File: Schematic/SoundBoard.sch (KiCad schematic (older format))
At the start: 0 parts

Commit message: Inital rev 1.0 commit
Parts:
- added C? (x8): 100n, symbol Device:C
- added C?: 10u, symbol Device:C
- added C? (x3): C, symbol Device:C
- added C? (x2): 2.2u, symbol Device:C
- added D?: D_Schottky, symbol Device:D_Schottky
- added D? (x3): LED, symbol Device:LED
- added F?: Fuse, symbol Device:Fuse
- added FB?: Ferrite_Bead, symbol Device:Ferrite_Bead
- added H? (x4): MountingHole_Pad, symbol Mechanical:MountingHole_Pad
- added J?: Conn_ARM_JTAG_SWD_10, symbol Connector:Conn_ARM_JTAG_SWD_10
- added LS?: Speaker, symbol Device:Speaker
- added R? (x5): R, symbol Device:R
- added SW? (x2): SW_Push, symbol Switch:SW_Push
- added U?: STM32F405RGTx, Package_QFP:LQFP-64_10x10mm_P0.5mm, symbol MCU_ST_STM32F4:STM32F405RGTx
- added U?: AMS1117-3.3, Package_TO_SOT_SMD:SOT-223-3_TabPin2, symbol Regulator_Linear:AMS1117-3.3
- added U? (x3): LM4562, symbol Amplifier_Operational:LM4562
- added U?: CS4344-CZZR, symbol SoundBoard:CS4344-CZZR
- added U?: W25Q128JVS, Package_SO:SOIC-8_5.23x5.23mm_P1.27mm, symbol Memory_Flash:W25Q128JVS
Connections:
- new net: C?.1, U?.31 (VCAP_1)
- new net: C?.1, U?.47 (VCAP_2)
- new net: C?.1, FB?.1, U?.3 (VI)
- new net: D?.1 (K), F?.2
- new net: F?.1, FB?.2
- new net: C?.1, LS?.1
- new net: D?.1 (K), R?.1 (x3)
- new net: J?.3 (GND), J?.5 (GND)
- new net +3V3: C?.1, C?.1, C?.1, C?.1, C?.1, C?.1, C?.1, C?.1, C?.1, C?.1, D?.2 (A), R?.1, R?.1, U?.1 (VBAT), U?.13 (VDDA), U?.19 (VDD), U?.2 (VO), U?.32 (VDD), U?.48 (VDD), U?.64 (VDD), U?.8 (V+), U?.9 (VA)
- new net BTN_1: R?.2, SW?.1
- new net BTN_2: R?.2, SW?.1
- new net GND: C?.2, C?.2, C?.2, C?.2, C?.2, C?.2, C?.2, C?.2, C?.2, C?.2, C?.2, C?.2, C?.2, H?.1, H?.1, H?.1, H?.1, LS?.2, R?.2, R?.2, R?.2, SW?.2, SW?.2, U?.1 (GND), U?.12 (VSSA), U?.18 (VSS), U?.4 (V-), U?.63 (VSS), U?.8 (GND)
- new net LED_1: D?.2 (A)
- new net LED_2: D?.2 (A)
- new net VDD: D?.2 (A)

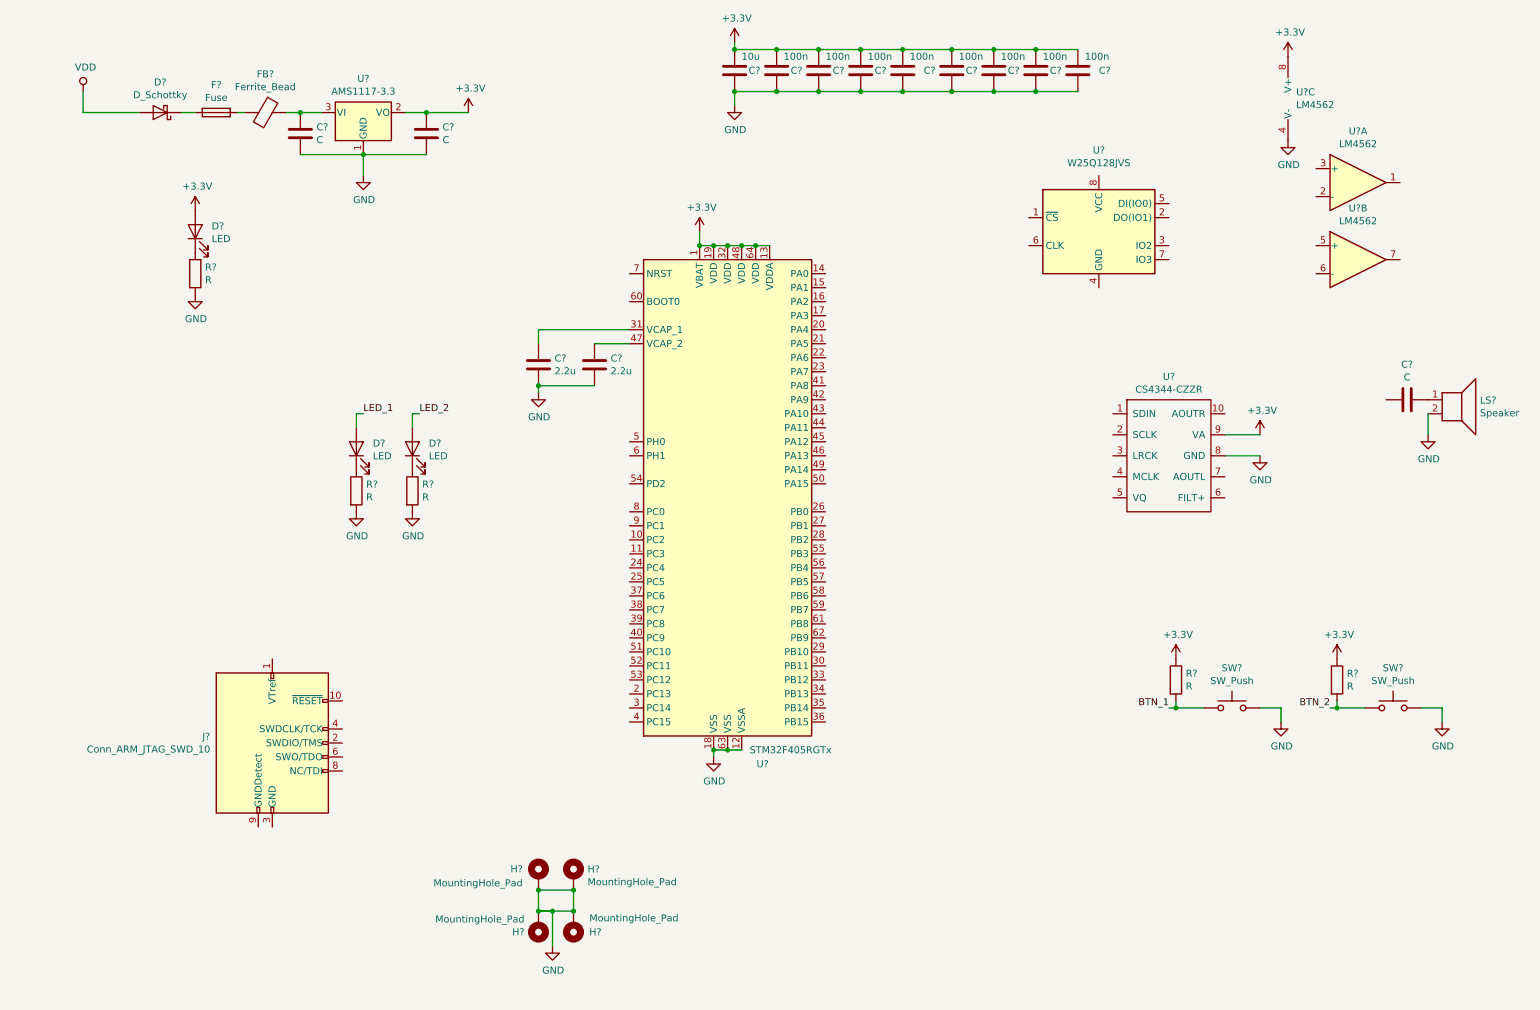
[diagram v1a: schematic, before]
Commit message: Footprint associations
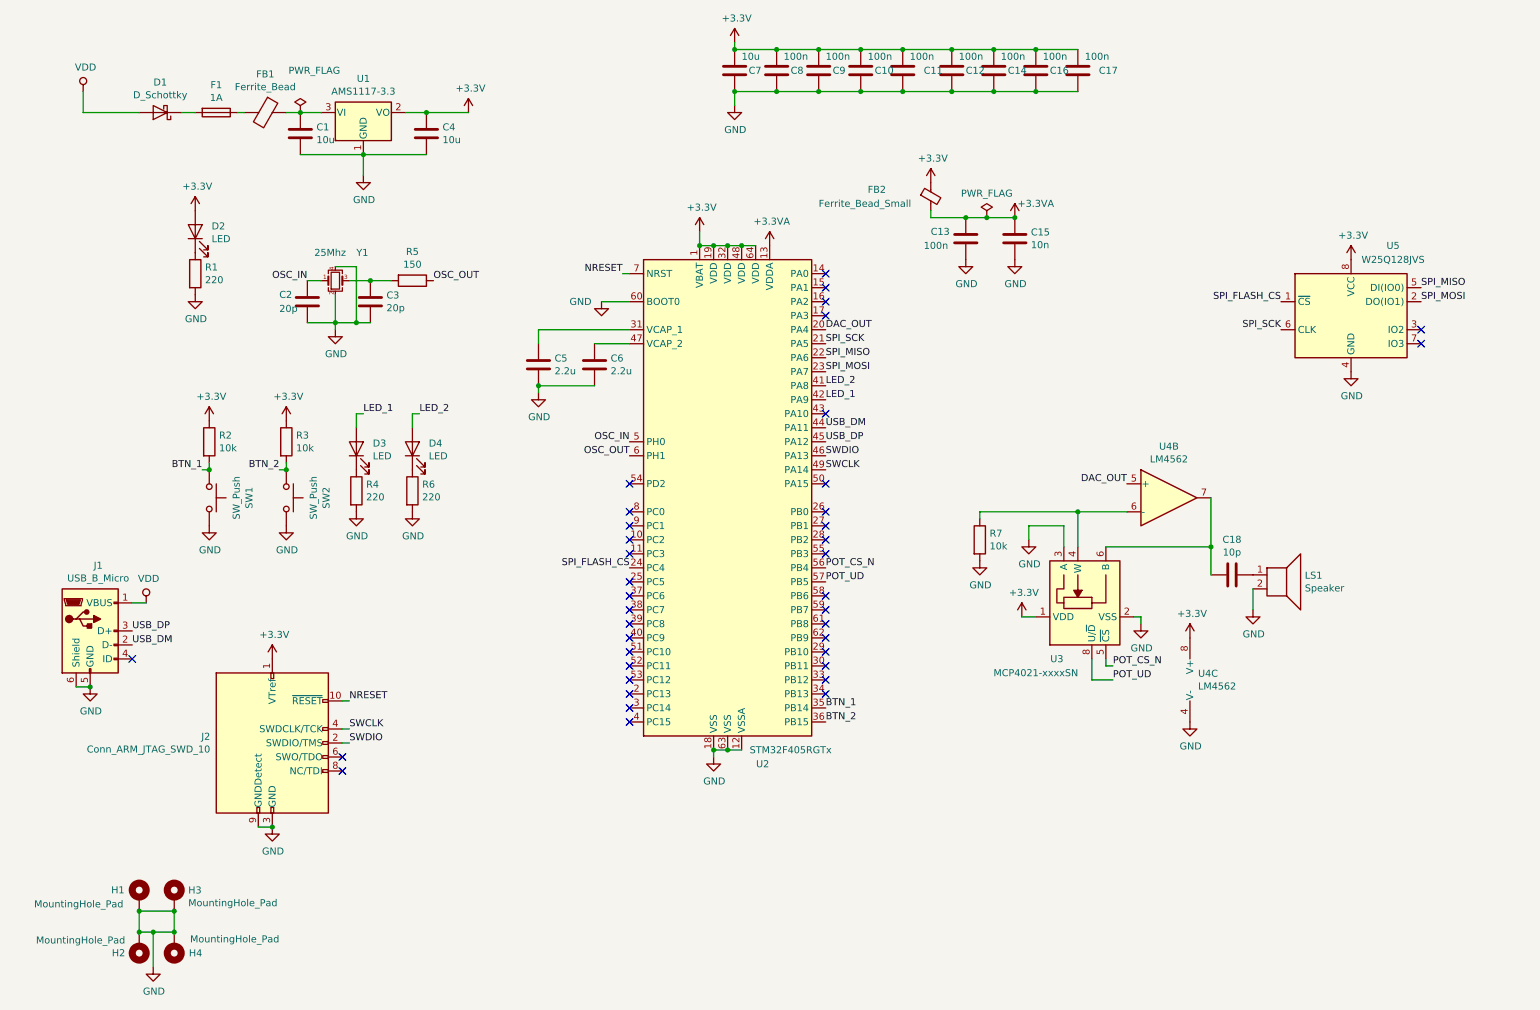
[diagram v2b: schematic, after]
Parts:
- removed U?: LM4562, symbol Amplifier_Operational:LM4562
- removed U?: CS4344-CZZR, symbol SoundBoard:CS4344-CZZR
- added C13: 100n, Capacitor_SMD:C_0603_1608Metric, symbol Device:C
- added C15: 10n, Capacitor_SMD:C_0603_1608Metric, symbol Device:C
- added C2, C3: 20p, Capacitor_SMD:C_0603_1608Metric, symbol Device:C
- added FB2: Ferrite_Bead_Small, Inductor_SMD:L_0603_1608Metric, symbol Device:Ferrite_Bead_Small
- added J1: USB_B_Micro, Connector_USB:USB_Micro-B_Amphenol_10103594-0001LF_Horizontal, symbol Connector:USB_B_Micro
- added R5: 150, Resistor_SMD:R_0603_1608Metric, symbol Device:R
- added R7: 10k, Resistor_SMD:R_0603_1608Metric, symbol Device:R
- added U3: MCP4021-xxxxSN, Package_SO:SOIC-8_3.9x4.9mm_P1.27mm, symbol Potentiometer_Digital:MCP4021-xxxxSN
- added Y1: 25Mhz, Crystal:Crystal_SMD_3225-4Pin_3.2x2.5mm, symbol Device:Crystal_GND24_Small
- C1, C4: renamed from C?; value C -> 10u; footprint (none) -> Capacitor_SMD:C_0603_1608Metric
- C10, C11, C12, C14, C16, C17, C5, C6, C7, C8, C9: renamed from C?; footprint (none) -> Capacitor_SMD:C_0603_1608Metric
- C18: renamed from C?; value C -> 10p; footprint (none) -> Capacitor_SMD:C_0603_1608Metric
- D1: renamed from D?; footprint (none) -> Diode_SMD:D_0603_1608Metric
- D2, D3, D4: renamed from D?; footprint (none) -> LED_SMD:LED_0603_1608Metric
- F1: renamed from F?; value Fuse -> 1A; footprint (none) -> Fuse:Fuse_0603_1608Metric
- FB1: renamed from FB?; footprint (none) -> Inductor_SMD:L_0603_1608Metric
- H1, H2, H3, H4: renamed from H?; footprint (none) -> MountingHole:MountingHole_4.3mm_M4_Pad
- J2: renamed from J?; footprint (none) -> Connector_PinHeader_1.27mm:PinHeader_2x05_P1.27mm_Vertical_SMD
- LS1: renamed from LS?; footprint (none) -> Soundboard:speaker_pads
- R1, R4, R6: renamed from R?; value R -> 220; footprint (none) -> Resistor_SMD:R_0603_1608Metric
- R2, R3: renamed from R?; value R -> 10k; footprint (none) -> Resistor_SMD:R_0603_1608Metric
- SW1, SW2: renamed from SW?; footprint (none) -> Button_Switch_SMD:SW_Push_1P1T_NO_6x6mm_H9.5mm
- U4: renamed from U?; footprint (none) -> Package_SO:SOIC-8_3.9x4.9mm_P1.27mm
- gave numbers to parts that had none: 3
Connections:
- net +3V3: now also J2.1 (VTref), U5.8 (VCC), FB2.1, U3.1 (VDD); no longer U2.13 (VDDA)
- net BTN_1: now also U2.35 (PB14)
- net BTN_2: now also U2.36 (PB15)
- net GND: now also J2.3 (GND), J2.5 (GND), J2.9 (GNDDetect), U2.60 (BOOT0), U5.4 (GND), C13.2, C15.2, C2.2, C3.2, J1.5 (GND), J1.6 (Shield), R7.2, U3.2 (VSS), U3.3 (A), Y1.2, Y1.4
- net LED_1: now also U2.42 (PA9)
- net LED_2: now also U2.41 (PA8)
- net VDD: now also J1.1 (VBUS)
- net DAC_OUT: now reaches U2.20 (PA4)
- net DAC_OUT: now also U4.5 (+)
- net SPI_SCK: now reaches U2.21 (PA5)
- net SPI_SCK: now also U5.6 (CLK)
- net SPI_MISO: now reaches U2.22 (PA6)
- net SPI_MISO: now also U5.5 (DI(IO0))
- net SPI_MOSI: now reaches U2.23 (PA7)
- net SPI_MOSI: now also U5.2 (DO(IO1))
- net SPI_FLASH_CS: now reaches U2.24 (PC4)
- net SPI_FLASH_CS: now also U5.1 (~CS)
- net USB_DM: now reaches U2.44 (PA11)
- net USB_DM: now also J1.2 (D-)
- net USB_DP: now reaches U2.45 (PA12)
- net USB_DP: now also J1.3 (D+)
- net SWDIO: now reaches U2.46 (PA13)
- net SWDIO: now also J2.2 (SWDIO/TMS)
- net SWCLK: now reaches U2.49 (PA14)
- net SWCLK: now also J2.4 (SWDCLK/TCK)
- net OSC_IN: now reaches U2.5 (PH0)
- net OSC_IN: now also C2.1, Y1.1
- net POT_CS_N: now reaches U2.56 (PB4)
- net POT_CS_N: now also U3.5 (~CS)
- net POT_UD: now reaches U2.57 (PB5)
- net POT_UD: now also U3.8 (U/~D)
- net OSC_OUT: now reaches U2.6 (PH1)
- net OSC_OUT: now also R5.1
- net NRESET: now reaches U2.7 (NRST)
- net NRESET: now also J2.10 (~RESET~)
- net at C18.2: now also U4.7, U3.6 (B)
- net at U4.6 (-): now also R7.1, U3.4 (W)
- new net: C3.1, R5.2, Y1.3
- new net +3.3VA: C13.1, C15.1, FB2.2, U2.13 (VDDA)
- no-connect marks 0 -> 39
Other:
- moved on the sheet: C18, H1, H2, H3, H4, LS1, R2, R3, SW1, SW2, U4B, U4C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
